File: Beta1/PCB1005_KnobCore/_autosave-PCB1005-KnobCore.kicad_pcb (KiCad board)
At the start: 2 copper layers, 160 x 50 mm, 33 parts, among them J1 Axoloti_40Pin, U1000 MCP3008T-I/SL, U2 MCP3008T-I/SL

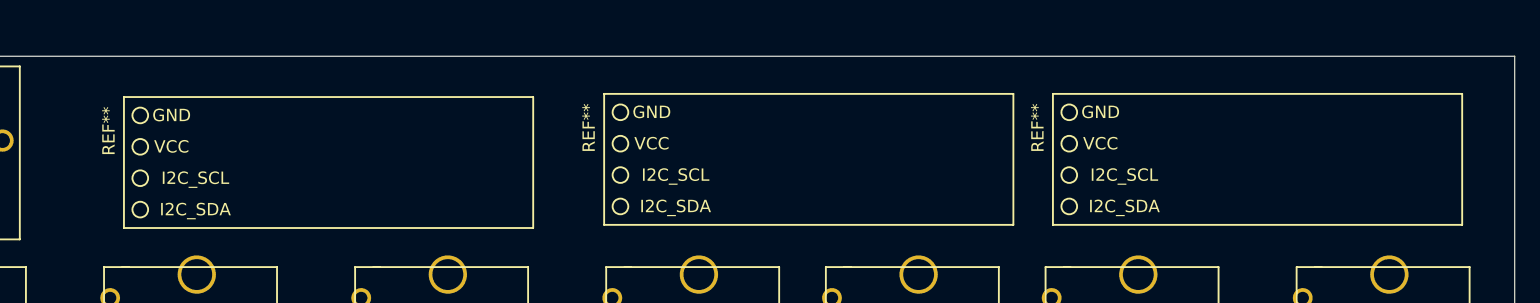
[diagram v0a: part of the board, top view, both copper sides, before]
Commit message: Added OLED to SCH. PCB needs update.
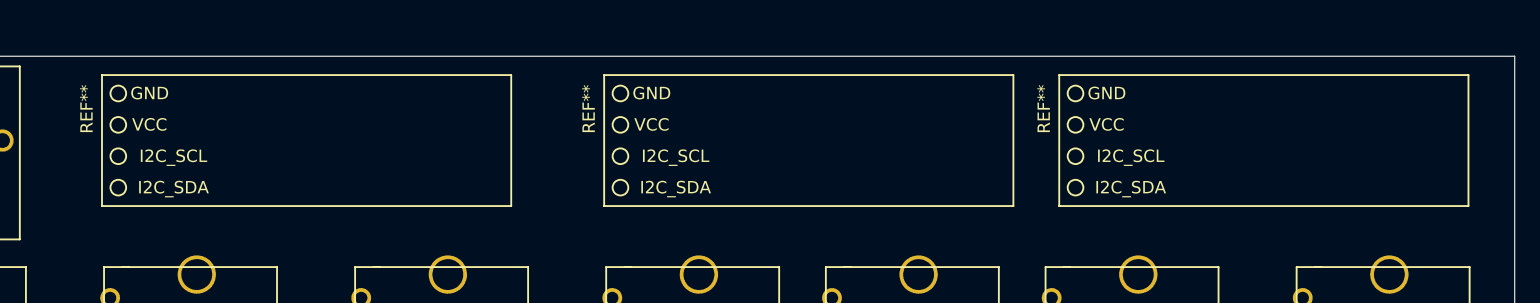
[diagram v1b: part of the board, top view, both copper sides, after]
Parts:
- moved REF** 2.51 mm to (62.2, -43.2)
- moved REF** 1.61 mm to (139.7, -43.2)
- moved REF** 1.52 mm to (102.9, -43.2)
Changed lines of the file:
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@@
     (mod_text_size 1 1)
     (mod_text_width 0.15)
-    (pad_size 1 1)
-    (pad_drill 0)
+    (pad_size 1.7272 1.7272)
+    (pad_drill 1.016)
     (pad_to_mask_clearance 0)
     (aux_axis_origin 0 0)
@@
   )
   (module Liberry:128x32_Footprint_guess (layer F.Cu)
-    (at 139.192 -41.656)
+    (at 139.7 -43.18)
     (fp_text reference REF** (at -17.78 -2.54 90) (layer F.SilkS)
       (effects (font (size 1 1) (thickness 0.15)))
@@
   )
   (module Liberry:128x32_Footprint_guess (layer F.Cu)
-    (at 102.87 -41.656)
+    (at 102.87 -43.18)
     (fp_text reference REF** (at -17.78 -2.54 90) (layer F.SilkS)
       (effects (font (size 1 1) (thickness 0.15)))
@@
   )
   (module Liberry:128x32_Footprint_guess (layer F.Cu)
-    (at 64.008 -41.402)
+    (at 62.23 -43.18)
     (fp_text reference REF** (at -17.78 -2.54 90) (layer F.SilkS)
       (effects (font (size 1 1) (thickness 0.15)))
